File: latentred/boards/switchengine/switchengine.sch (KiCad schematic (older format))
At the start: 0 parts

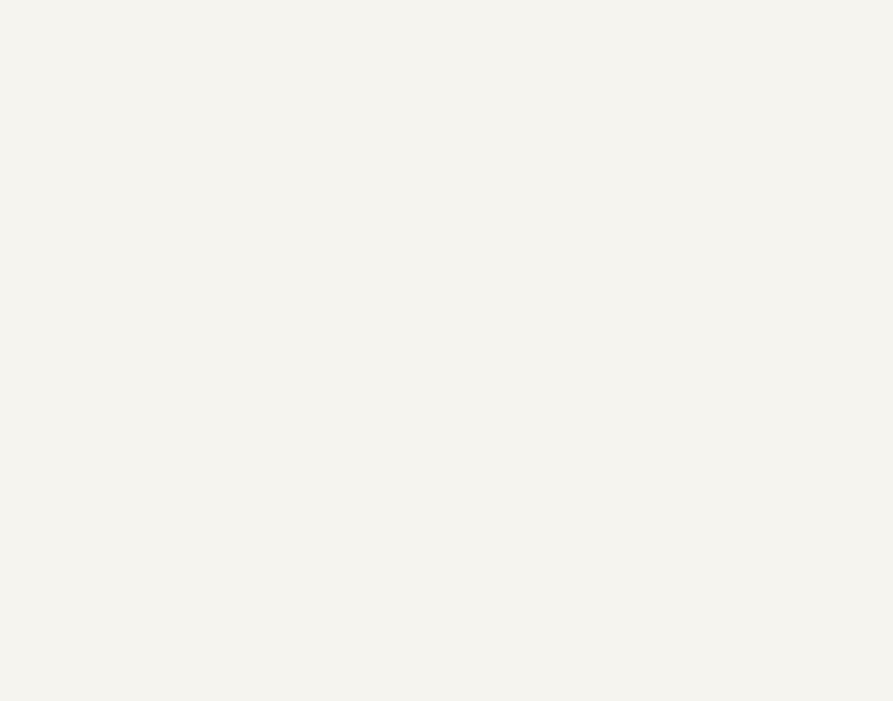
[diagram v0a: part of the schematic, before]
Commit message: Continued initial work on switch engine schematic and power budgeting
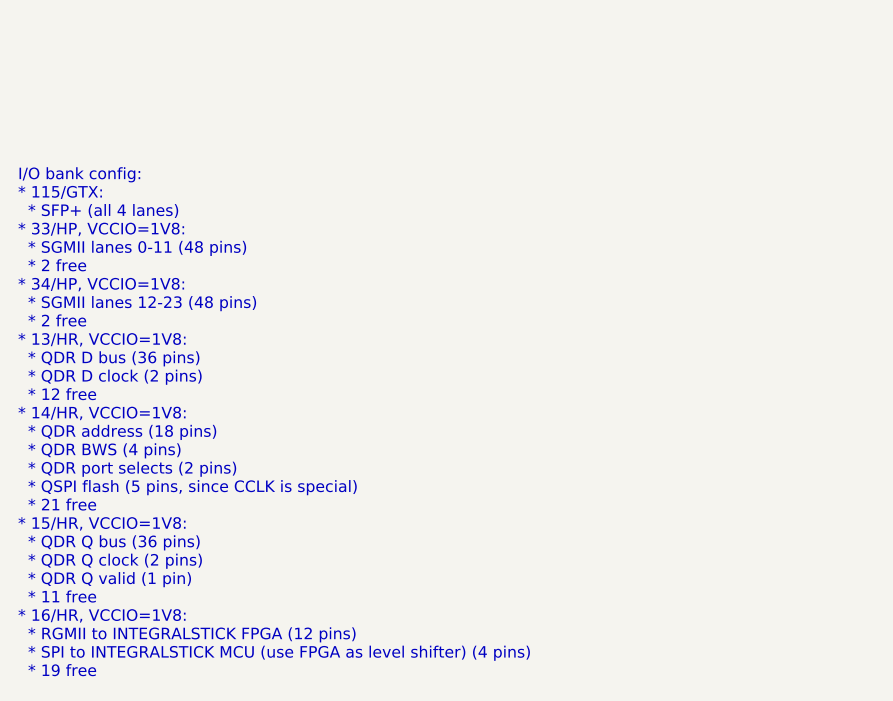
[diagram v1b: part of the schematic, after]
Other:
- note added: "I/O bank config:\n* 115/GTX:\n * SFP+ (all 4 lanes)\n* 33/HP, VCCIO=1V8:\n * SGMII lanes 0-11 (48 pins)\n * 2 free\n* 34/HP, VCCIO=1V8:\n * SGMII lanes 12-23 (48 pins)\n * 2 free\n* 13/HR, VCCIO=1V8:\n * QDR D bus (36 pins)\n * QDR D clock (2 pins)\n * 12 free\n* 14/HR, VCCIO=1V8:\n * QDR address (18 pins)\n * QDR BWS (4 pins)\n * QDR port selects (2 pins)\n * QSPI flash (5 pins, since CCLK is sp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"
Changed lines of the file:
@@
 $Descr A4 11693 8268
 encoding utf-8
-Sheet 1 5
+Sheet 1 6
 Title "LATENTRED Switch Engine"
 Date "2019-09-09"
@@
 F1 "fpga-support.sch" 50
 $EndSheet
+Text Notes 800  7250 0    50   ~ 0
+I/O bank config:\n* 115/GTX:\n  * SFP+ (all 4 lanes)\n* 33/HP, VCCIO=1V8:\n  * SGMII lanes 0-11 (48 pins)\n  * 2 free\n* 34/HP, VCCIO=1V8:\n  * SGMII lanes 12-23 (48 pins)\n  * 2 free\n* 13/HR, VCCIO=1V8:\n  * QDR D bus (36 pins)\n  * QDR D clock (2 pins)\n  * 12 free\n* 14/HR, VCCIO=1V8:\n  * QDR address (18 pins)\n  * QDR BWS (4 pins)\n  * QDR port selects (2 pins)\n  * QSPI flash (5 pins, since CCLK is special)\n  * 21 free\n* 15/HR, VCCIO=1V8:\n  * QDR Q bus (36 pins)\n  * QDR Q clock (2 pins)\n  * QDR Q valid (1 pin) \n  * 11 free\n* 16/HR, VCCIO=1V8:\n  * RGMII to INTEGRALSTICK FPGA (12 pins)\n  * SPI to INTEGRALSTICK MCU (use FPGA as level shifter) (4 pins)\n  * 19 free
 $EndSCHEMATC
